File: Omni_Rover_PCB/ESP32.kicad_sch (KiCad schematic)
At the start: 25 parts, among them J1 Conn_01x04_Socket, Q1 SS8050, Q2 SS8050, SW1 TSA016A2526A, SW2 TSA016A2526A, U3 CH340C, U4 ESP32-WROOM-32D

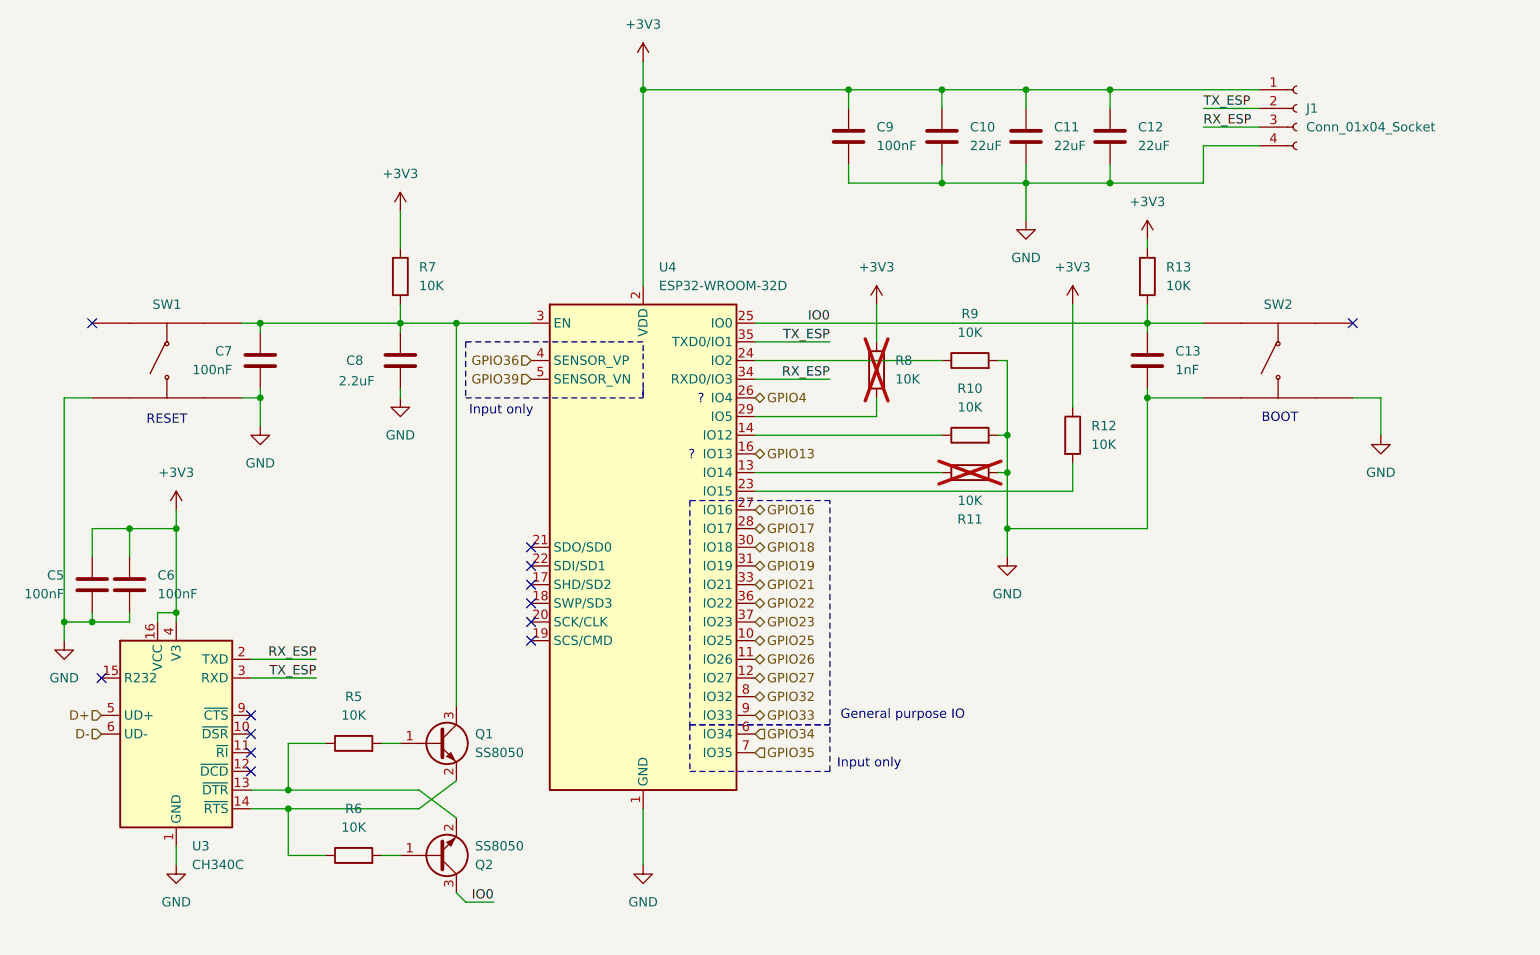
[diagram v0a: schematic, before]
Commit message: Finished the Laout 0 DRC ERRORS. Just needs some finishing touches.
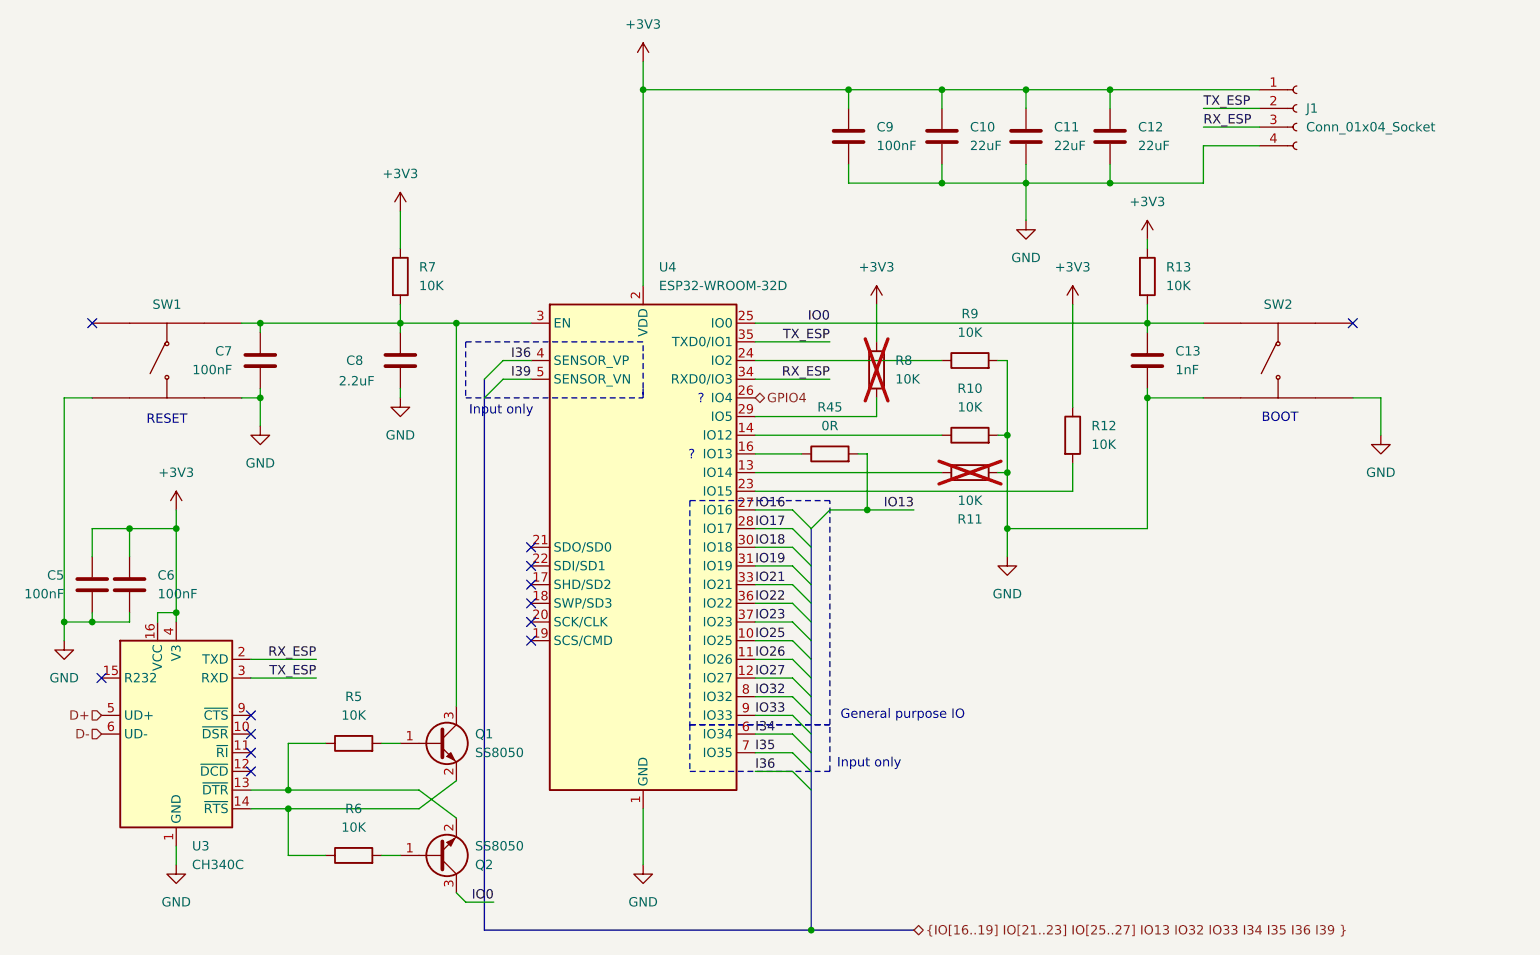
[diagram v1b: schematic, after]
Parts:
- added R45: 0R, Resistor_SMD:R_0402_1005Metric_Pad0.72x0.64mm_HandSolder, symbol Device:R
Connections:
- net GPIO13: no longer names the net of U4.16 (IO13)
- net GPIO13: now also R45.1
- net GPIO16 renamed IO16
- net GPIO17 renamed IO17
- net GPIO18 renamed IO18
- net GPIO19 renamed IO19
- net GPIO21 renamed IO21
- net GPIO22 renamed IO22
- net GPIO23 renamed IO23
- net GPIO25 renamed IO25
- net GPIO26 renamed IO26
- net GPIO27 renamed IO27
- net GPIO32 renamed IO32
- net GPIO33 renamed IO33
- net GPIO34 renamed I34
- net GPIO35 renamed I35
- net GPIO36 renamed I36
- net GPIO39 renamed I39
- new net IO13: R45.2

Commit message: Made soem minor fixes to the schematic and PCB layout.
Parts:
- added C67: 22uF, Capacitor_SMD:C_0805_2012Metric_Pad1.18x1.45mm_HandSolder, symbol Device:C
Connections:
- net +3V3: now also C67.1
- net GND: now also C67.2
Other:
- moved on the sheet: C10, C11, C12, C9
